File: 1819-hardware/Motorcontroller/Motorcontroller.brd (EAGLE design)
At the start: 38.1 x 38.7 mm, 31 parts, among them U1 GENERIC-SOIC8MSGEQ7N-FILTER, U2 GENERIC-SOIC8MSGEQ7N-FILTER, U3 GENERIC-SOIC8MSGEQ7N-FILTER, U4 PCA9685

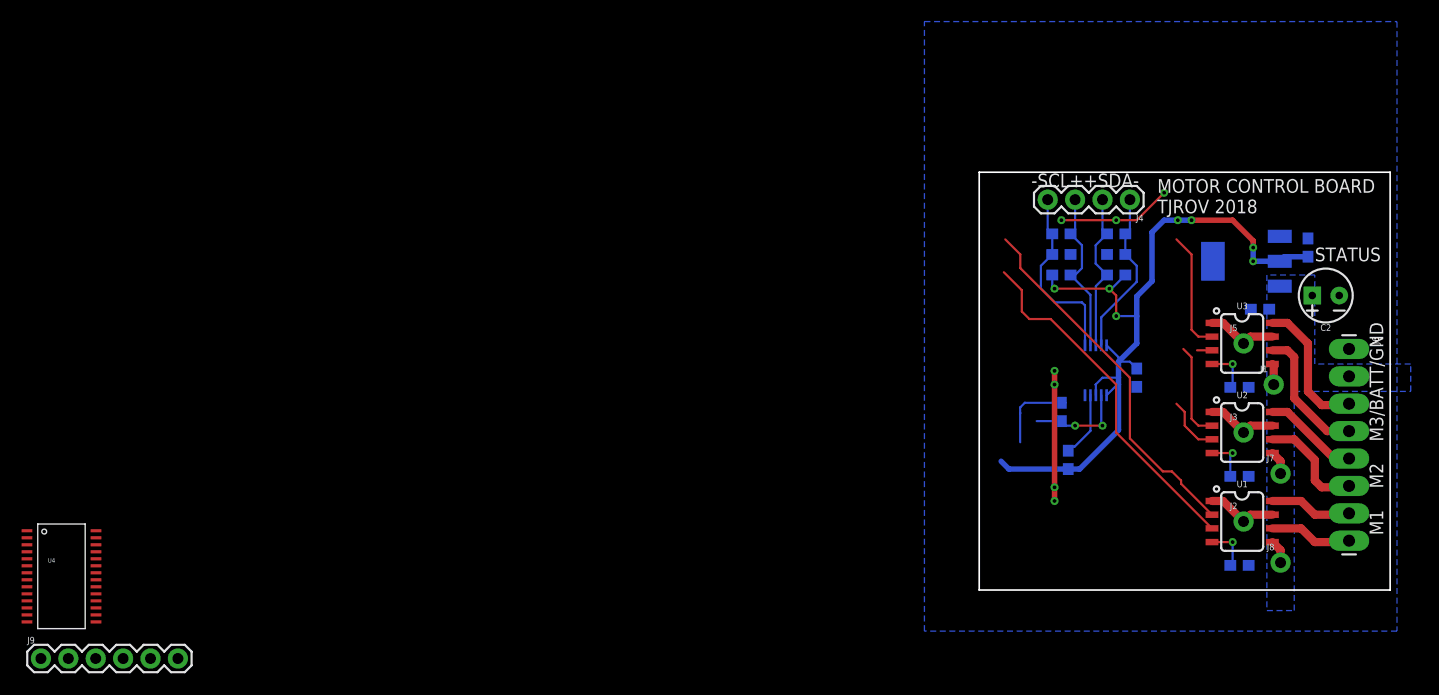
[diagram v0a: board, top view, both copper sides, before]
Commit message: component positions done
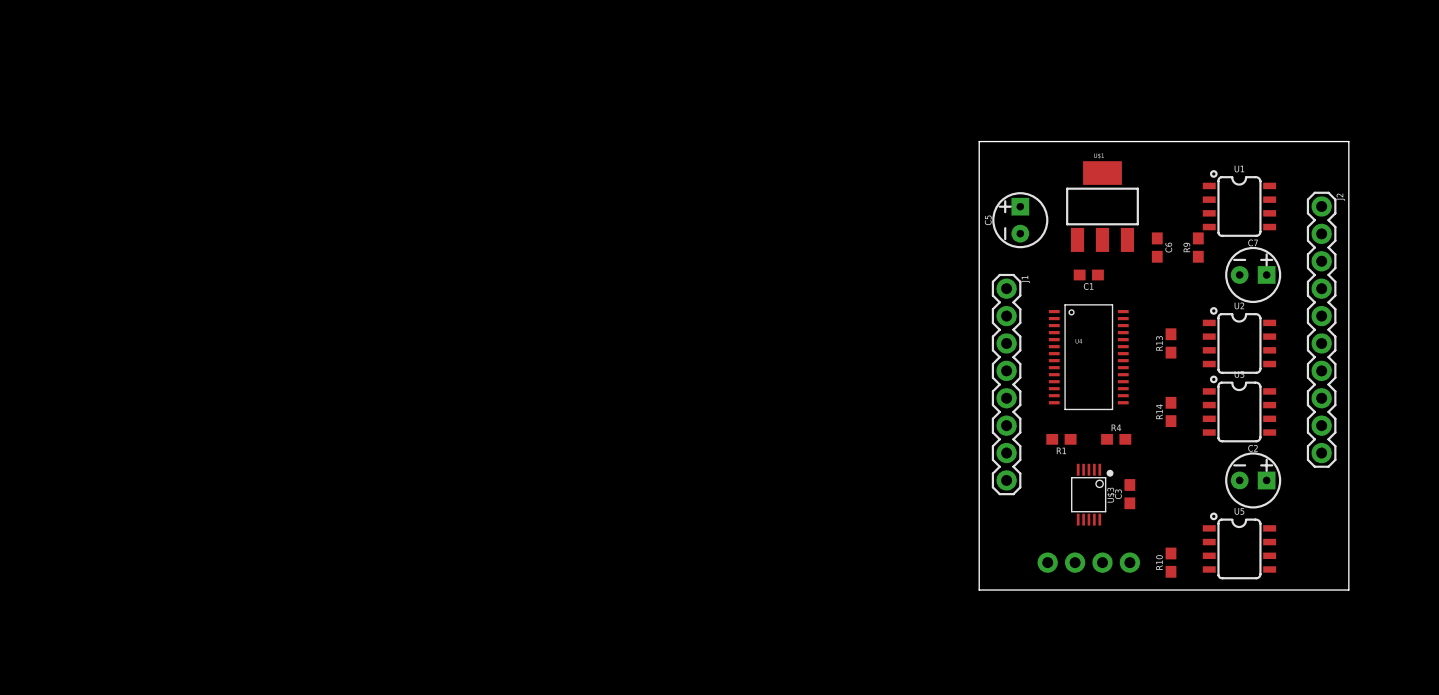
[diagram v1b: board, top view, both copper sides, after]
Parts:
- removed J3, J5, J7, J8: (no value), SparkFun-Connectors:1X01_NO_SILK
- removed J6: (no value), SparkFun-Connectors:1X08_LONGPADS
- removed J9: (no value), SparkFun-Connectors:1X06
- removed R2, R3: 100, SparkFun-Resistors:0603
- removed R5, R6, R7, R8: 680, SparkFun-Resistors:0603
- added C5, C7: 10uF, SparkFun-Capacitors:CPOL-RADIAL-2.5MM-5MM
- added R10: 47k, SparkFun-Resistors:0603
- added U5: GENERIC-SOIC8MSGEQ7N-FILTER, SparkFun-Retired:SO08
- J1: device SparkFun-Connectors:1X01_NO_SILK -> SparkFun-Connectors:1X08
- J2: device SparkFun-Connectors:1X01_NO_SILK -> SparkFun-Connectors:1X10
- moved U4 97.4 mm to (10.2, 21.6)
- moved FRAME1 41.9 mm to (-38.1, 47.0)
- moved J4 33.7 mm to (14.0, 2.54), flipped to the bottom, turned to 0 degrees
- moved J2 30.1 mm to (31.8, 35.6), turned to 270 degrees
- moved R9 29.7 mm to (20.3, 31.8), flipped to the top, turned to 90 degrees
- moved U1 29.2 mm to (24.1, 35.6)
- moved J1 26.3 mm to (2.54, 27.9), turned to 270 degrees
- moved C1 20.5 mm to (10.2, 29.2), flipped to the top, turned to 180 degrees
- moved C2 18.4 mm to (25.4, 10.2), turned to 0 degrees
- moved U$1 14.3 mm to (11.4, 35.6), flipped to the top, turned to 0 degrees
- moved R13 13.9 mm to (17.8, 22.9), flipped to the top, turned to 90 degrees
- moved U$3 11.4 mm to (10.2, 8.89), flipped to the top, turned to 270 degrees
- moved C6 11.1 mm to (16.5, 31.8), flipped to the top, turned to 270 degrees
- moved C3 10.8 mm to (14.0, 8.89), flipped to the top, turned to 90 degrees
- moved U2 8.26 mm to (24.1, 22.9)
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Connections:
- removed net M1IN1: U1.3
- removed net M1IN2: U1.2
- removed net M1OUT1: J6.8, U1.6
- removed net M1OUT2: J6.7, U1.8
- removed net M2IN1: U2.3
- removed net M2IN2: U2.2
- removed net M2OUT1: J6.6, U2.6
- removed net M2OUT2: J6.5, U2.8
- removed net M3IN1: U3.3
- removed net M3IN2: U3.2
- removed net M3OUT1: J6.4, U3.6
- removed net M3OUT2: J6.3, U3.8
- removed net N$10: U4.19
- removed net N$11: U4.18
- removed net N$12: U4.17
- removed net N$13: U4.16
- removed net N$14: U4.15
- removed net N$15: U4.14
- removed net N$16: U4.13
- removed net N$17: U4.12
- removed net N$18: U4.11
- removed net N$19: U4.10
- removed net N$20: U4.9
- removed net N$21: U4.8
- removed net N$22: U4.7
- removed net N$23: U4.6
- removed net N$24: U4.5
- removed net N$25: U4.4
- removed net N$26: U4.3
- removed net N$27: U4.2
- removed net N$28: U4.1
- removed net N$29: U4.24
- removed net N$30: U4.23
- removed net N$4: U4.27
- removed net N$5: U4.26
- removed net N$6: U4.22
- removed net N$8: U4.21
- removed net N$9: U4.20
- new net ESC0: J1.1, U4.6
- new net ESC7: J1.8, U4.13
- new net M0-A: U1.2, U4.22
- new net M0-B: U1.3, U4.21
- new net M0-OUTA: J2.3, U1.8
- new net M0-OUTB: J2.4, U1.6
- new net M1-A: U2.2, U4.20
- new net M1-B: U2.3, U4.19
- new net M1-OUTA: J2.5, U2.8
- new net M1-OUTB: J2.6, U2.6
- new net M2-A: U3.2, U4.18
- new net M2-B: U3.3, U4.17
- new net M2-OUTA: J2.7, U3.8
- new net M2-OUTB: J2.8, U3.6
- new net M3-A: U4.16, U5.2
- new net M3-B: U4.15, U5.3
- new net M3-OUTA: J2.9, U5.8
- new net M3-OUTB: J2.10, U5.6
- net BATT: now also C7.1, J2.2, U5.5; no longer J1.1, J6.2, J7.1, J8.1
- net ESC1: now also J1.2, U4.7; no longer J9.1
- net ESC2: now also J1.3, U4.8; no longer J9.2
- net ESC3: now also J1.4, U4.9; no longer J9.3
- net ESC4: now also J1.5, U4.10; no longer J9.4
- net ESC5: now also J1.6, U4.11; no longer J9.5
- net ESC6: now also J1.7, U4.12; no longer J9.6
- net GND: now also C5.2, C7.2, R10.1, U4.1, U4.14, U4.2, U4.23, U4.24, U4.25, U4.3, U4.4, U4.5, U5.1, U5.7; no longer J3.1, J5.1, J6.1, R5.1, R6.1
- net N$3: now also R10.2, U5.4; no longer U4.28
- net SCL: now also U4.26
- net SCL+: no longer R3.2, R7.1
- net SCL-: no longer R3.1, R6.2
- net SDA: now also U4.27
- net SDA+: no longer R2.2, R8.1
- net SDA-: no longer R2.1, R5.2
- net VCC: now also C5.1, U4.28; no longer R7.2, R8.2
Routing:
- net VCC: track 79.7 -> 0.00 mm, vias 7 -> 0
- net GND: track 42.6 -> 0.00 mm, vias 7 -> 0
- net M1IN2: track 34.0 -> 0.00 mm
- net M1IN1: track 32.9 -> 0.00 mm
- net SCL-: track 17.3 -> 0.00 mm
- net SCL+: track 15.6 -> 0.00 mm
- net SDA-: track 15.5 -> 0.00 mm
- net SDA+: track 15.0 -> 0.00 mm
- net M3OUT2: track 12.9 -> 0.00 mm
- net M3OUT1: track 12.4 -> 0.00 mm
- net M3IN2: track 11.1 -> 0.00 mm
- net M2OUT1: track 10.1 -> 0.00 mm
- net SDA: track 9.15 -> 0.00 mm, vias 2 -> 0
- net M2IN2: track 8.95 -> 0.00 mm
- net M2OUT2: track 8.89 -> 0.00 mm
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- removed copper zone on layer 16, net BATT
- removed copper zone on layer 16, net GND
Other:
- board size 38.1 x 38.7 mm -> 34.3 x 41.6 mm
- board text removed: "-SCL++SDA-"
- board text removed: "M1 M2 M3/BATT/GND"
- board text removed: "MOTOR CONTROL BOARD TJROV 2018"
- board text removed: "STATUS"

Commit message: motorcontroller board
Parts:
- added J3, J5, J6, J7: (no value), SparkFun-Connectors:1X01_NO_SILK
- moved R14 6.84 mm to (20.3, 10.2)
- moved R13 2.54 mm to (17.8, 20.3)
- moved R9 2.54 mm to (20.3, 29.2)
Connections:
- net BATT: now also J2.10; no longer J2.2
- net GND: now also J3.1, J5.1, J6.1, J7.1
- net M0-OUTA: now also J2.2; no longer J2.3
- net M0-OUTB: now also J2.3; no longer J2.4
- net M1-OUTA: now also J2.4; no longer J2.5
- net M1-OUTB: now also J2.5; no longer J2.6
- net M2-OUTA: now also J2.6; no longer J2.7
- net M2-OUTB: now also J2.7; no longer J2.8
- net M3-OUTA: now also J2.8; no longer J2.9
- net M3-OUTB: now also J2.9; no longer J2.10
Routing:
- added copper zone on layer 1, net BATT
- added copper zone on layer 16, net BATT
- added copper zone on layer 16, net GND

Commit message: more work on boards
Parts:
- removed J2: (no value), SparkFun-Connectors:1X10
- added J10, J9: (no value), SparkFun-Connectors:1X02
- added J11, J8: 455-1750-1-ND, SparkFun-Connectors:1X03
- moved R1 1.80 mm to (8.89, 15.2)
- moved R4 1.27 mm to (12.7, 15.2)
- moved U4 1.27 mm to (10.2, 22.9)
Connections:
- net BATT: now also J11.3; no longer J2.10
- net GND: now also J8.1; no longer J2.1
- net M0-OUTA: now also J8.2; no longer J2.2
- net M0-OUTB: now also J8.3; no longer J2.3
- net M1-OUTA: now also J9.1; no longer J2.4
- net M1-OUTB: now also J9.2; no longer J2.5
- net M2-OUTA: now also J10.1; no longer J2.6
- net M2-OUTB: now also J10.2; no longer J2.7
- net M3-OUTA: now also J11.1; no longer J2.8
- net M3-OUTB: now also J11.2; no longer J2.9
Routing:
- net VCC: track 0.00 -> 52.8 mm, vias 0 -> 2
- net GND: track 0.00 -> 49.7 mm, vias 0 -> 4
- net BATT: track 0.00 -> 13.7 mm, vias 12 -> 9
- net SDA-: track 0.00 -> 5.72 mm
- net M3-OUTB: track 0.00 -> 5.61 mm
- net M3-OUTA: track 0.00 -> 5.61 mm
- net SCL-: track 0.00 -> 5.15 mm
- net M0-OUTA: track 0.00 -> 5.08 mm
- net M2-OUTB: track 0.00 -> 5.08 mm
- net M2-OUTA: track 0.00 -> 5.08 mm
- net M1-OUTB: track 0.00 -> 5.08 mm
- net M1-OUTA: track 0.00 -> 5.08 mm
- net M0-OUTB: track 0.00 -> 5.08 mm
- net SDA+: track 0.00 -> 4.50 mm
- net SCL+: track 0.00 -> 4.31 mm

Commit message: motorcontroller routng done
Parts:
- moved R4 4.02 mm to (8.89, 16.5), turned to 180 degrees
- moved R1 1.90 mm to (8.89, 13.3)
- moved R13 1.27 mm to (17.8, 19.1)
- turned R10 to 270 degrees
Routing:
- net M0-A: track 0.00 -> 20.4 mm, vias 0 -> 2
- net M3-B: track 0.00 -> 20.3 mm
- net M3-A: track 0.00 -> 19.7 mm
- net M0-B: track 0.00 -> 19.4 mm, vias 0 -> 2
- net SDA: track 0.00 -> 18.2 mm
- net SCL: track 0.00 -> 16.7 mm, vias 0 -> 2
- net GND: track 49.7 -> 66.3 mm, vias 4 -> 6
- net ESC7: track 0.00 -> 11.5 mm
- net M2-B: track 0.00 -> 11.1 mm
- net M2-A: track 0.00 -> 10.5 mm
- net ESC6: track 0.00 -> 9.65 mm
- net M1-A: track 0.00 -> 8.64 mm
- net M1-B: track 0.00 -> 8.38 mm
- net ESC5: track 0.00 -> 8.12 mm
- net ESC0: track 0.00 -> 7.61 mm
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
